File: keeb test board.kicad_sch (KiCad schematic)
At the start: 15 parts, among them SW12 SW_Push, SW14 SW_Push, SW15 SW_Push, SW3 SW_Push, SW6 SW_Push, SW9 SW_Push, U1 BluePill_V1.1

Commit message: Routing improvements
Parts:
- H1, H2, H3, H4: footprint MountingHole:MountingHole_2.2mm_M2_DIN965 -> Keeby-Cat Footprints:MountingHole_2.2mm_M2_DIN965
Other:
- moved on the sheet: H1, H2, H3, H4
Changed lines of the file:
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@@
     (pin "1")
   )
-  (symbol (lib_id "Mechanical:MountingHole") (at 135.89 64.77 0) (unit 1)
-    (in_bom yes) (on_board yes) (fields_autoplaced)
-    (property "Reference" "H2" (id 0) (at 138.43 63.4999 0)
-      (effects (font (size 1.27 1.27)) (justify left))
-    )
-    (property "Value" "MountingHole" (id 1) (at 138.43 66.0399 0)
-      (effects (font (size 1.27 1.27)) (justify left))
-    )
-    (property "Footprint" "MountingHole:MountingHole_2.2mm_M2_DIN965" (id 2) (at 135.89 64.77 0)
-      (effects (font (size 1.27 1.27)) hide)
-    )
-    (property "Datasheet" "~" (id 3) (at 135.89 64.77 0)
+  (symbol (lib_id "Mechanical:MountingHole") (at 135.89 65.278 0) (unit 1)
+    (in_bom yes) (on_board yes) (fields_autoplaced)
+    (property "Reference" "H2" (id 0) (at 138.43 64.0079 0)
+      (effects (font (size 1.27 1.27)) (justify left))
+    )
+    (property "Value" "MountingHole" (id 1) (at 138.43 66.5479 0)
+      (effects (font (size 1.27 1.27)) (justify left))
+    )
+    (property "Footprint" "Keeby-Cat Footprints:MountingHole_2.2mm_M2_DIN965" (id 2) (at 135.89 65.278 0)
+      (effects (font (size 1.27 1.27)) hide)
+    )
+    (property "Datasheet" "~" (id 3) (at 135.89 65.278 0)
       (effects (font (size 1.27 1.27)) hide)
     )
@@
     (pin "4")
   )
-  (symbol (lib_id "Mechanical:MountingHole") (at 135.89 71.12 0) (unit 1)
-    (in_bom yes) (on_board yes) (fields_autoplaced)
-    (property "Reference" "H4" (id 0) (at 138.43 69.8499 0)
-      (effects (font (size 1.27 1.27)) (justify left))
-    )
-    (property "Value" "MountingHole" (id 1) (at 138.43 72.3899 0)
-      (effects (font (size 1.27 1.27)) (justify left))
-    )
-    (property "Footprint" "MountingHole:MountingHole_2.2mm_M2_DIN965" (id 2) (at 135.89 71.12 0)
-      (effects (font (size 1.27 1.27)) hide)
-    )
-    (property "Datasheet" "~" (id 3) (at 135.89 71.12 0)
+  (symbol (lib_id "Mechanical:MountingHole") (at 135.89 71.628 0) (unit 1)
+    (in_bom yes) (on_board yes) (fields_autoplaced)
+    (property "Reference" "H4" (id 0) (at 138.43 70.3579 0)
+      (effects (font (size 1.27 1.27)) (justify left))
+    )
+    (property "Value" "MountingHole" (id 1) (at 138.43 72.8979 0)
+      (effects (font (size 1.27 1.27)) (justify left))
+    )
+    (property "Footprint" "Keeby-Cat Footprints:MountingHole_2.2mm_M2_DIN965" (id 2) (at 135.89 71.628 0)
+      (effects (font (size 1.27 1.27)) hide)
+    )
+    (property "Datasheet" "~" (id 3) (at 135.89 71.628 0)
       (effects (font (size 1.27 1.27)) hide)
     )
@@
     (pin "2")
   )
-  (symbol (lib_id "Mechanical:MountingHole") (at 110.49 64.77 0) (unit 1)
-    (in_bom yes) (on_board yes) (fields_autoplaced)
-    (property "Reference" "H1" (id 0) (at 113.03 63.4999 0)
-      (effects (font (size 1.27 1.27)) (justify left))
-    )
-    (property "Value" "MountingHole" (id 1) (at 113.03 66.0399 0)
-      (effects (font (size 1.27 1.27)) (justify left))
-    )
-    (property "Footprint" "MountingHole:MountingHole_2.2mm_M2_DIN965" (id 2) (at 110.49 64.77 0)
-      (effects (font (size 1.27 1.27)) hide)
-    )
-    (property "Datasheet" "~" (id 3) (at 110.49 64.77 0)
+  (symbol (lib_id "Mechanical:MountingHole") (at 110.49 65.278 0) (unit 1)
+    (in_bom yes) (on_board yes) (fields_autoplaced)
+    (property "Reference" "H1" (id 0) (at 113.03 64.0079 0)
+      (effects (font (size 1.27 1.27)) (justify left))
+    )
+    (property "Value" "MountingHole" (id 1) (at 113.03 66.5479 0)
+      (effects (font (size 1.27 1.27)) (justify left))
+    )
+    (property "Footprint" "Keeby-Cat Footprints:MountingHole_2.2mm_M2_DIN965" (id 2) (at 110.49 65.278 0)
+      (effects (font (size 1.27 1.27)) hide)
+    )
+    (property "Datasheet" "~" (id 3) (at 110.49 65.278 0)
       (effects (font (size 1.27 1.27)) hide)
     )
@@
     (pin "1")
   )
-  (symbol (lib_id "Mechanical:MountingHole") (at 110.49 71.12 0) (unit 1)
-    (in_bom yes) (on_board yes) (fields_autoplaced)
-    (property "Reference" "H3" (id 0) (at 113.03 69.8499 0)
-      (effects (font (size 1.27 1.27)) (justify left))
-    )
-    (property "Value" "MountingHole" (id 1) (at 113.03 72.3899 0)
-      (effects (font (size 1.27 1.27)) (justify left))
-    )
-    (property "Footprint" "MountingHole:MountingHole_2.2mm_M2_DIN965" (id 2) (at 110.49 71.12 0)
-      (effects (font (size 1.27 1.27)) hide)
-    )
-    (property "Datasheet" "~" (id 3) (at 110.49 71.12 0)
+  (symbol (lib_id "Mechanical:MountingHole") (at 110.49 71.628 0) (unit 1)
+    (in_bom yes) (on_board yes) (fields_autoplaced)
+    (property "Reference" "H3" (id 0) (at 113.03 70.3579 0)
+      (effects (font (size 1.27 1.27)) (justify left))
+    )
+    (property "Value" "MountingHole" (id 1) (at 113.03 72.8979 0)
+      (effects (font (size 1.27 1.27)) (justify left))
+    )
+    (property "Footprint" "Keeby-Cat Footprints:MountingHole_2.2mm_M2_DIN965" (id 2) (at 110.49 71.628 0)
+      (effects (font (size 1.27 1.27)) hide)
+    )
+    (property "Datasheet" "~" (id 3) (at 110.49 71.628 0)
       (effects (font (size 1.27 1.27)) hide)
     )
@@
     )
     (path "/d7dc8332-4e7d-4d1c-9e13-94700025e229"
-      (reference "H1") (unit 1) (value "MountingHole") (footprint "MountingHole:MountingHole_2.2mm_M2_DIN965")
+      (reference "H1") (unit 1) (value "MountingHole") (footprint "Keeby-Cat Footprints:MountingHole_2.2mm_M2_DIN965")
     )
     (path "/5a7e5e4b-0f2c-4c71-9d32-45cf0732b0c3"
-      (reference "H2") (unit 1) (value "MountingHole") (footprint "MountingHole:MountingHole_2.2mm_M2_DIN965")
+      (reference "H2") (unit 1) (value "MountingHole") (footprint "Keeby-Cat Footprints:MountingHole_2.2mm_M2_DIN965")
     )
     (path "/f81e2caa-f7a2-40dd-8668-c447b8223c0a"
-      (reference "H3") (unit 1) (value "MountingHole") (footprint "MountingHole:MountingHole_2.2mm_M2_DIN965")
+      (reference "H3") (unit 1) (value "MountingHole") (footprint "Keeby-Cat Footprints:MountingHole_2.2mm_M2_DIN965")
     )
     (path "/8ea18563-8d92-48ab-81f4-e90c6181f6de"
-      (reference "H4") (unit 1) (value "MountingHole") (footprint "MountingHole:MountingHole_2.2mm_M2_DIN965")
+      (reference "H4") (unit 1) (value "MountingHole") (footprint "Keeby-Cat Footprints:MountingHole_2.2mm_M2_DIN965")
     )
     (path "/6ce8230c-595b-49b4-b7e1-27c56bb79809/368da0b2-4a09-4c1c-a7bd-9829d431f181"

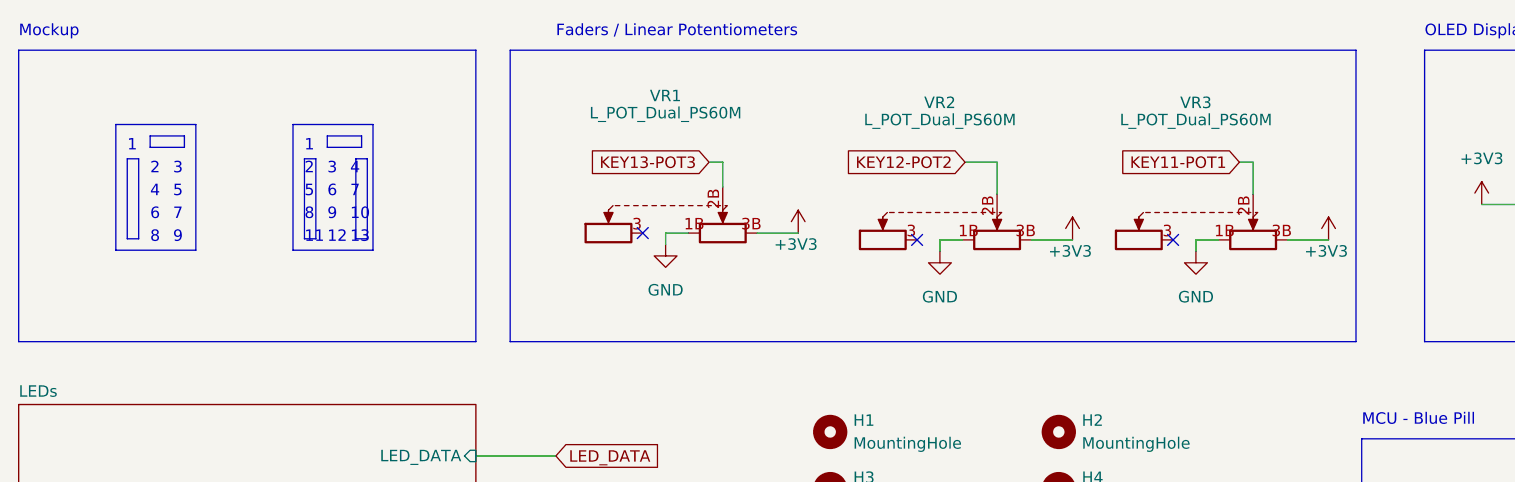
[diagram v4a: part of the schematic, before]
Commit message: Fixed pin-sharing faders/keys
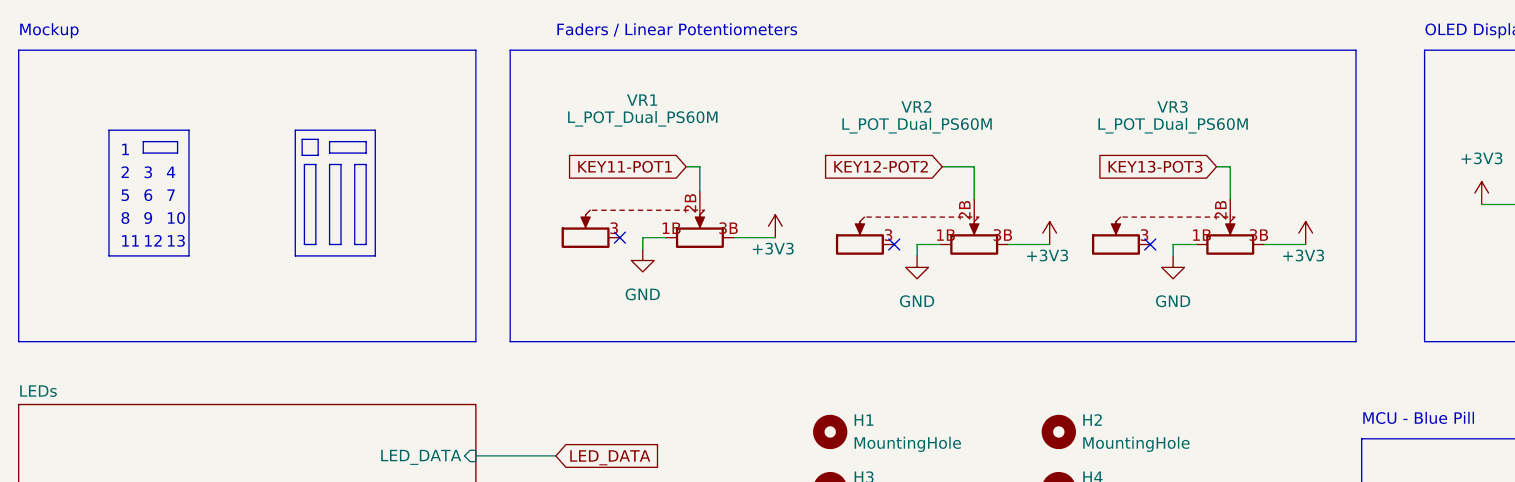
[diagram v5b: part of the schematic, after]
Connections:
- net KEY11-POT1: now also VR1.2B; no longer VR3.2B
- net KEY13-POT3: now also VR3.2B; no longer VR1.2B
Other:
- moved on the sheet: VR1, VR2, VR3

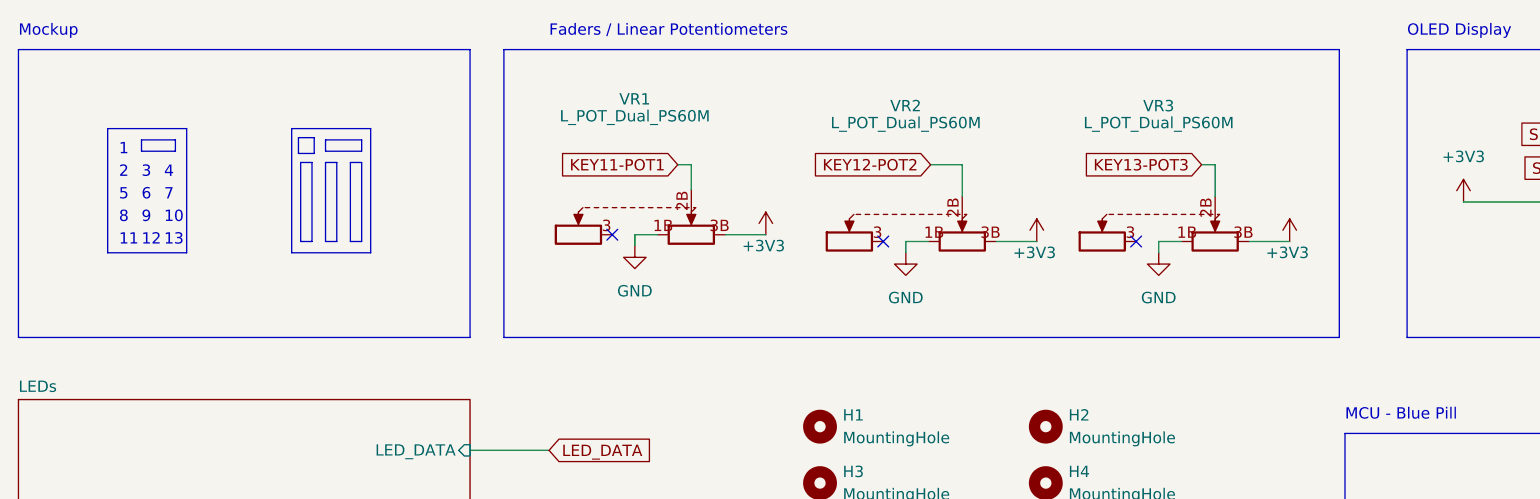
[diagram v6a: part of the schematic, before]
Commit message: Centered faders and rotated LEDs
Experimental solution to make faders centered to lower 4 rows of keys/grid. Requires bending or trimming off an unused pin from the faders.
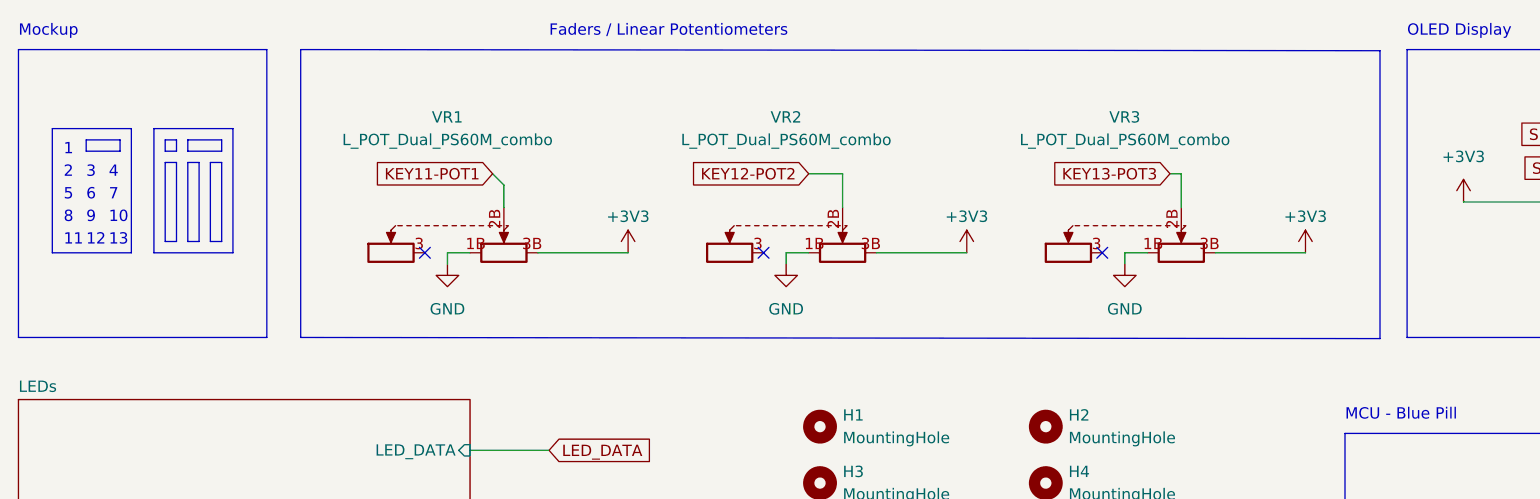
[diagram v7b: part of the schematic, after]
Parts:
- VR1, VR2, VR3: value L_POT_Dual_PS60M -> L_POT_Dual_PS60M_combo
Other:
- moved on the sheet: VR1, VR2, VR3

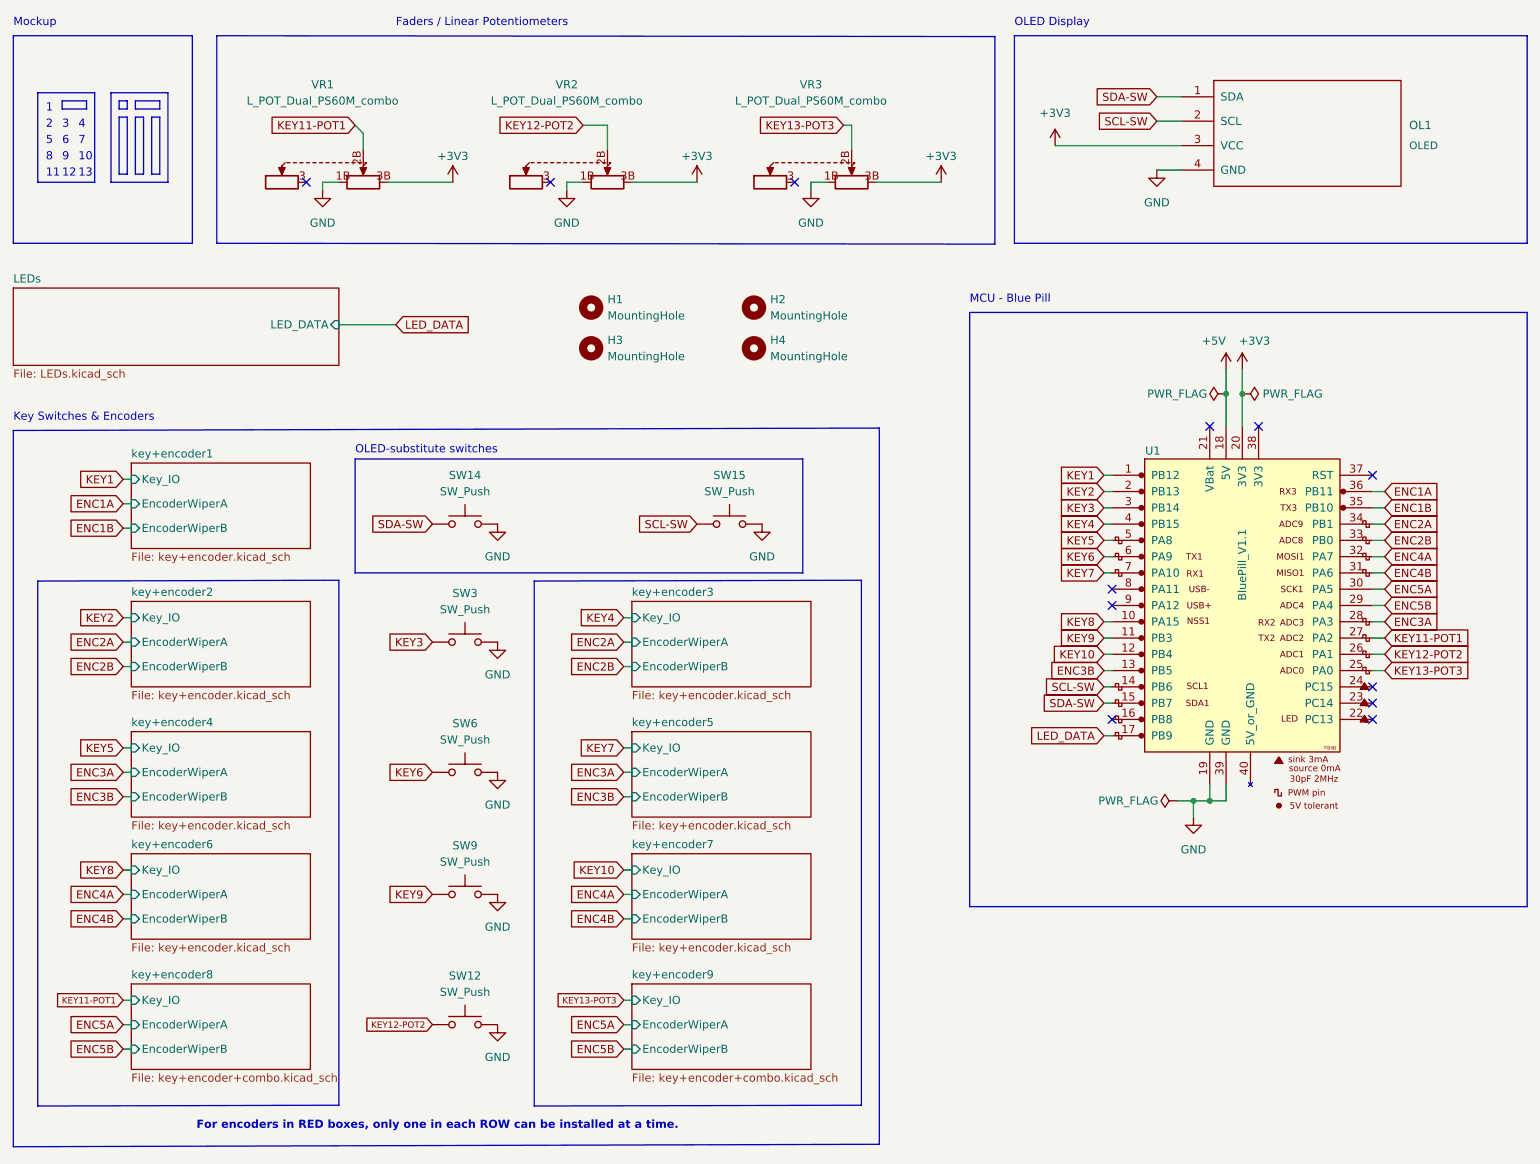
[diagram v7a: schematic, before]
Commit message: routing and footprint fixes
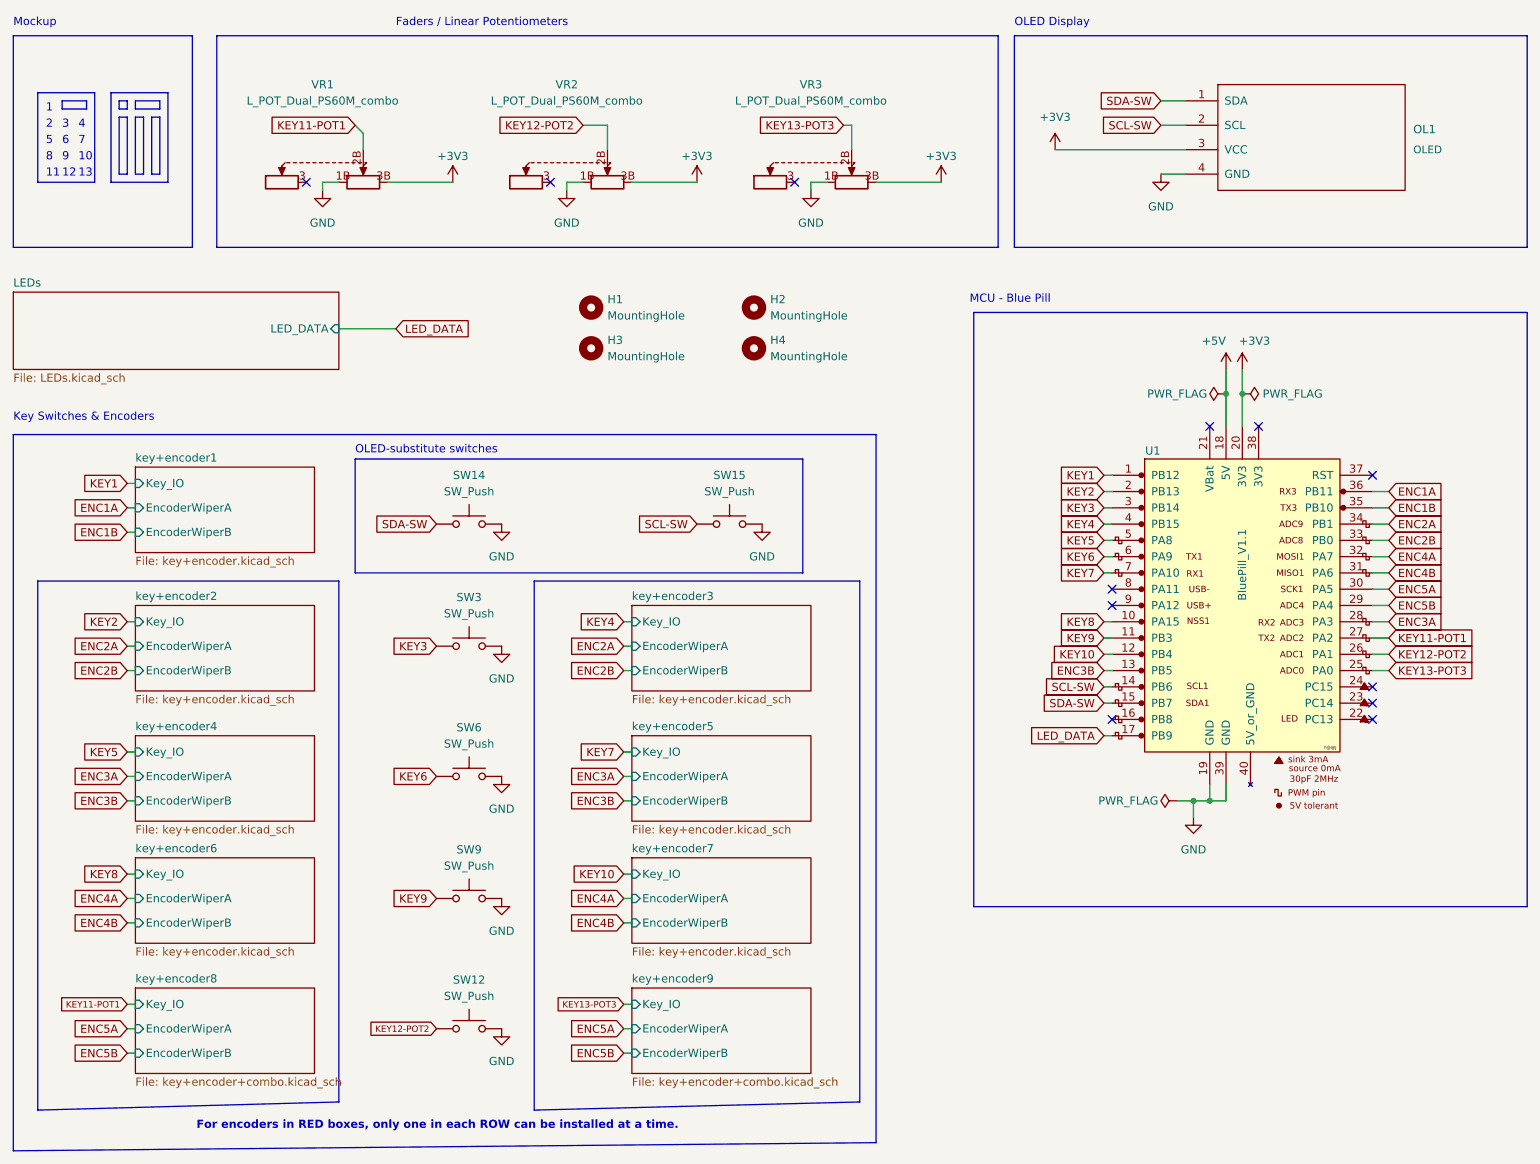
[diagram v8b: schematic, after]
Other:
- moved on the sheet: OL1, SW12, SW14, SW3, SW6, SW9
